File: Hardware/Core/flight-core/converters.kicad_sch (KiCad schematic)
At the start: 16 parts, among them U113 Fuse_Holder_Blade, U12 18-75V to 5V Converter, U4 TPS62086RLTR, U80 3.3V VCC Current Sensor, U81 5V VCC Current Sensor, U82 Fuse_Holder_Blade

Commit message: added common mode filter on CAN term resistor; renamed cube_ok
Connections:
- net POWER_ENABLE: now reaches U12.2 (ON/OFF)
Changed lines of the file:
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@@
+		)
+	)
+	(hierarchical_label "POWER_ENABLE"
+		(shape input)
+		(at 58.42 71.12 180)
+		(effects
+			(font
+				(size 1.27 1.27)
+			)
+			(justify right)
 		)
 	)

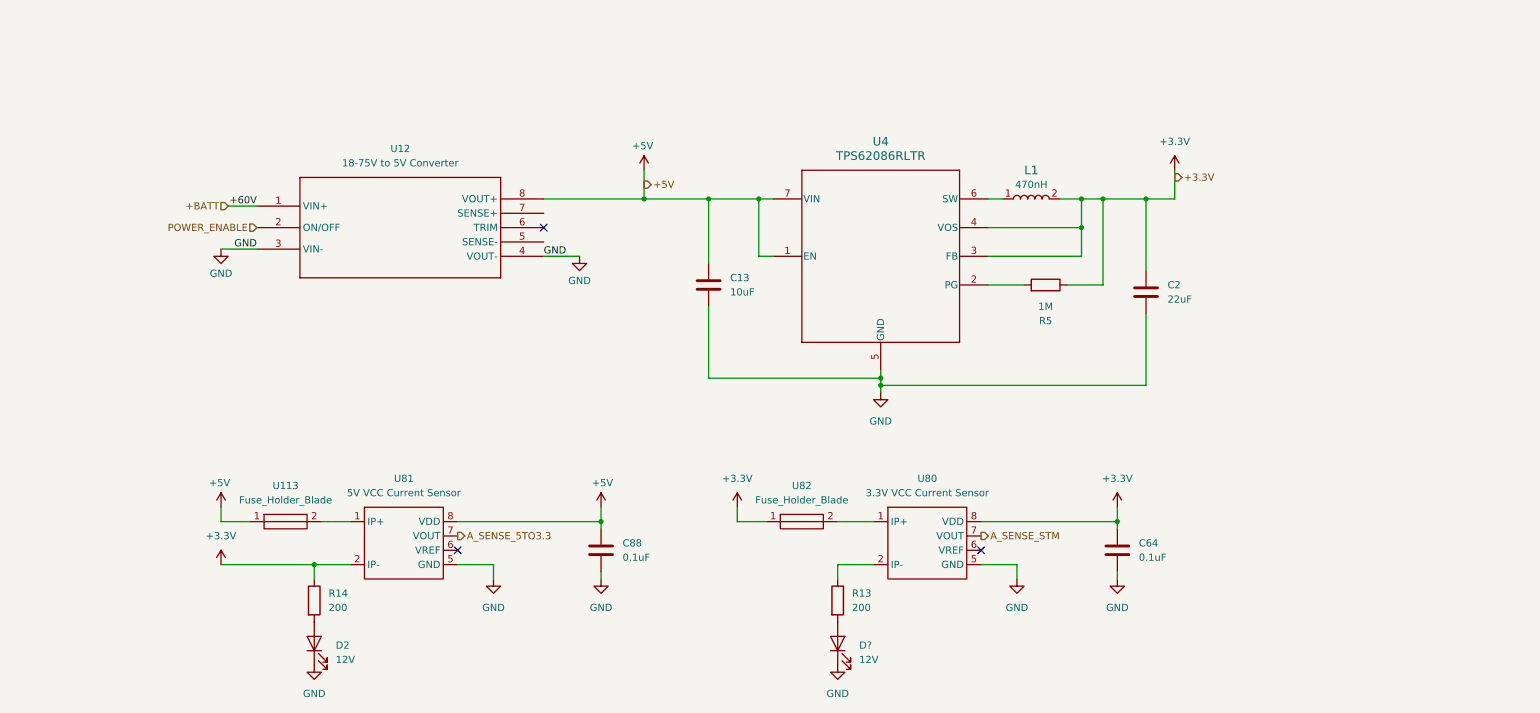
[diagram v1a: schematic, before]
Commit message: adding in-progress converter enable; in-lined shunt resistors, source 5V from USB, LEDs moved
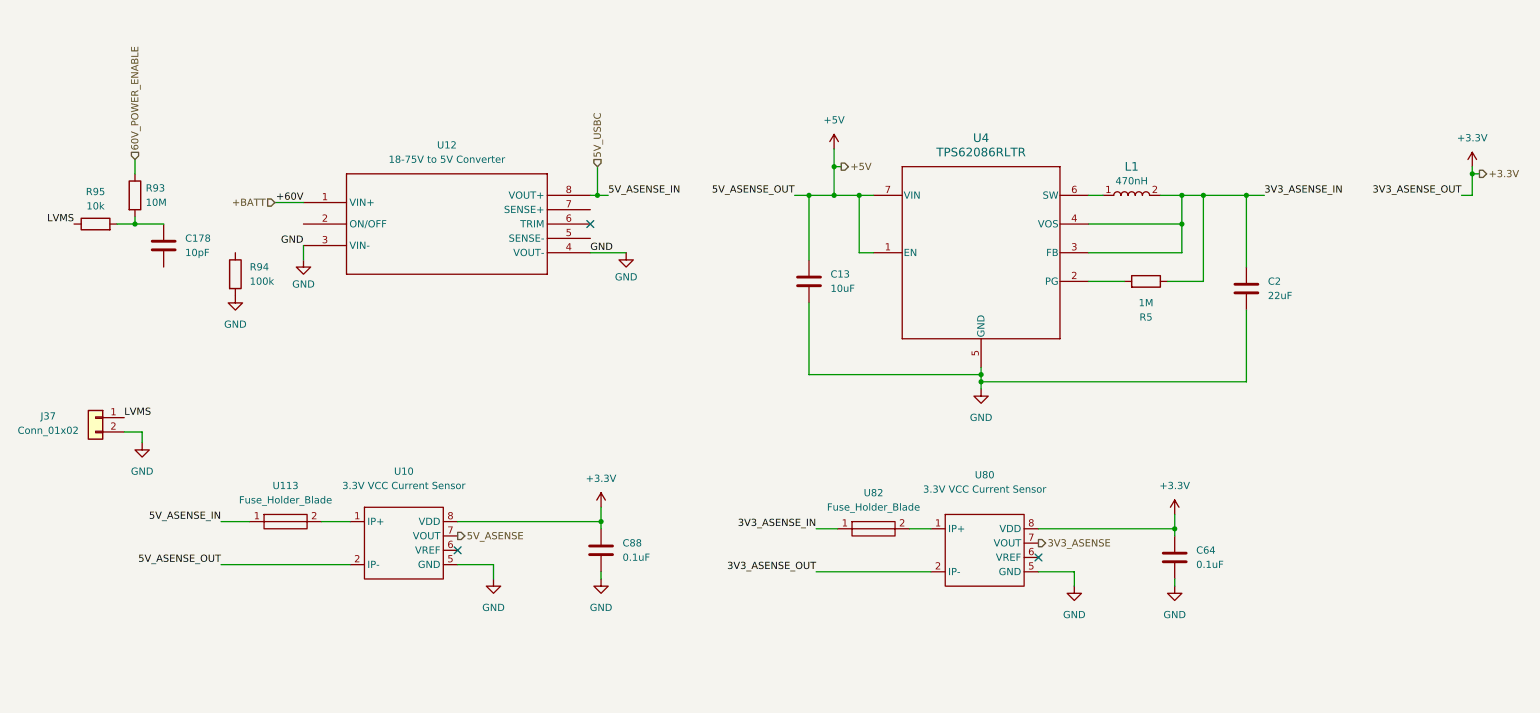
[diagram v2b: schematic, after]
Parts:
- removed D2, D?: 12V, footprints:LED_0805_OEM, symbol oem:LED_0805
- removed R13, R14: 200, OEM:R_0603, symbol OEM:R_200
- removed U81: 5V VCC Current Sensor, obad_footprints:U_Current-Sensor_ACS37010LLZATR-030B5_SOIC-6, symbol OlinBAD:ACS37010LLZATR-030B5
- added C178: 10pF, footprints:C_0603_1608Metric, symbol Device:C
- added J37: Conn_01x02, symbol Connector_Generic:Conn_01x02
- added R93: 10M, footprints:R_0603_1608Metric, symbol Device:R
- added R94: 100k, footprints:R_0603_1608Metric, symbol Device:R
- added R95: 10k, footprints:R_0603_1608Metric, symbol Device:R
- added U10: 3.3V VCC Current Sensor, obad_footprints:U_Current-Sensor_ACS37010LLZATR-030B5_SOIC-6, symbol OlinBAD:ACS37010LLZATR-030B3
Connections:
- net +3.3V: now also C88.1, U80.2 (IP-), U10.8 (VDD); no longer C2.1, L1.2, R5.1, U4.3 (FB), U4.4 (VOS), U82.1
- net +5V: now also U10.2 (IP-); no longer C88.1, U113.1, U12.8 (VOUT+)
- net GND: now also J37.2 (Pin_2), R94.2, U10.5 (GND)
- net at U113.2: now also U10.1 (IP+)
- net A_SENSE_STM renamed 3V3_ASENSE
- net POWER_ENABLE: no longer names the net of U12.2 (ON/OFF)
- new net: C178.1, R93.2, R95.2
- new net 3V3_ASENSE_IN: C2.1, L1.2, R5.1, U4.3 (FB), U4.4 (VOS), U82.1
- new net 5V_ASENSE: U10.7 (VOUT)
- new net 5V_USBC: U113.1, U12.8 (VOUT+)
- new net 60V_POWER_ENABLE: R93.1
- new net LVMS: J37.1 (Pin_1), R95.1
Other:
- moved on the sheet: C13, C2, C64, L1, R5, U12, U4, U80, U82

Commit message: top sheet reorg
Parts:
- removed J37: Conn_01x02, symbol Connector_Generic:Conn_01x02
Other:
- moved on the sheet: C13, C178, C2, C64, C88, L1, R5, R93, R94, R95, U10, U113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

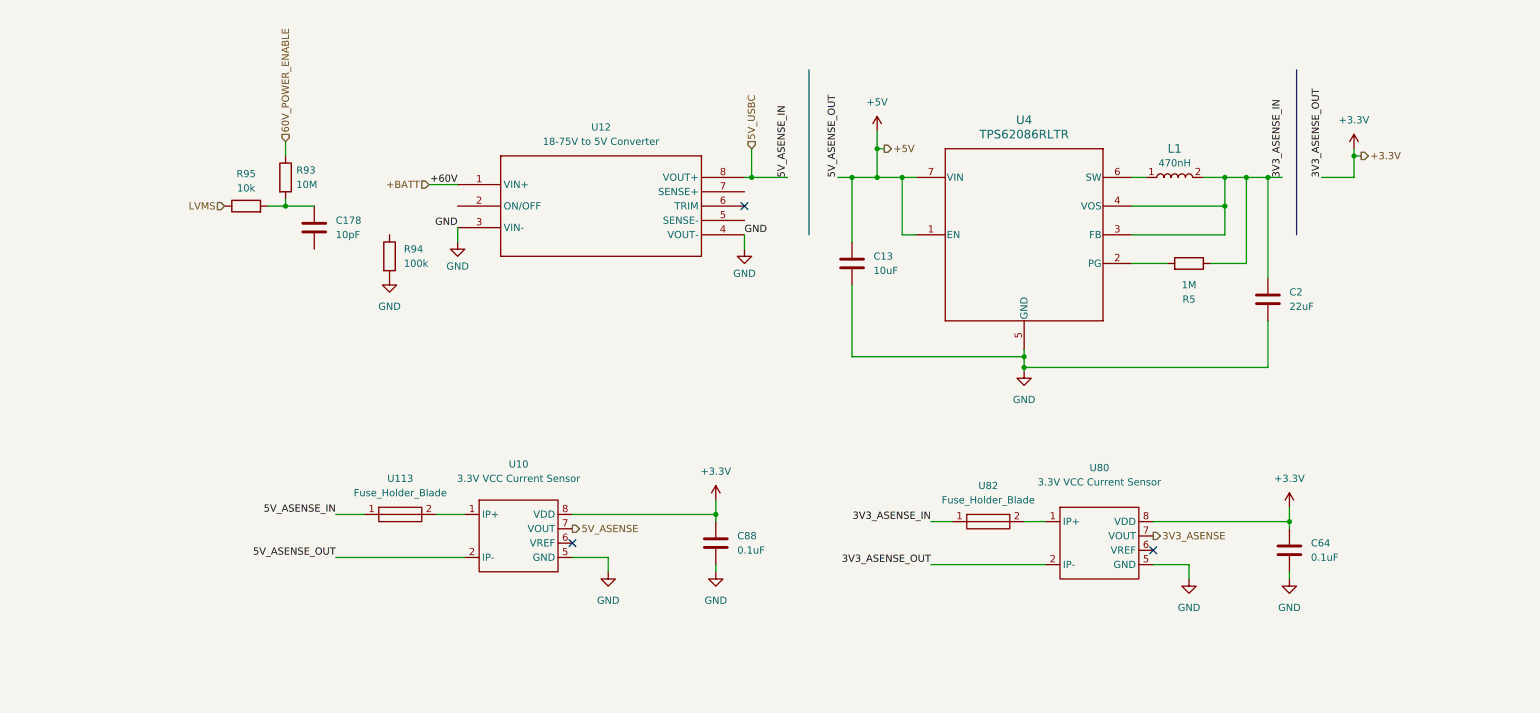
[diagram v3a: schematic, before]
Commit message: updated shutdown and some aux circuits
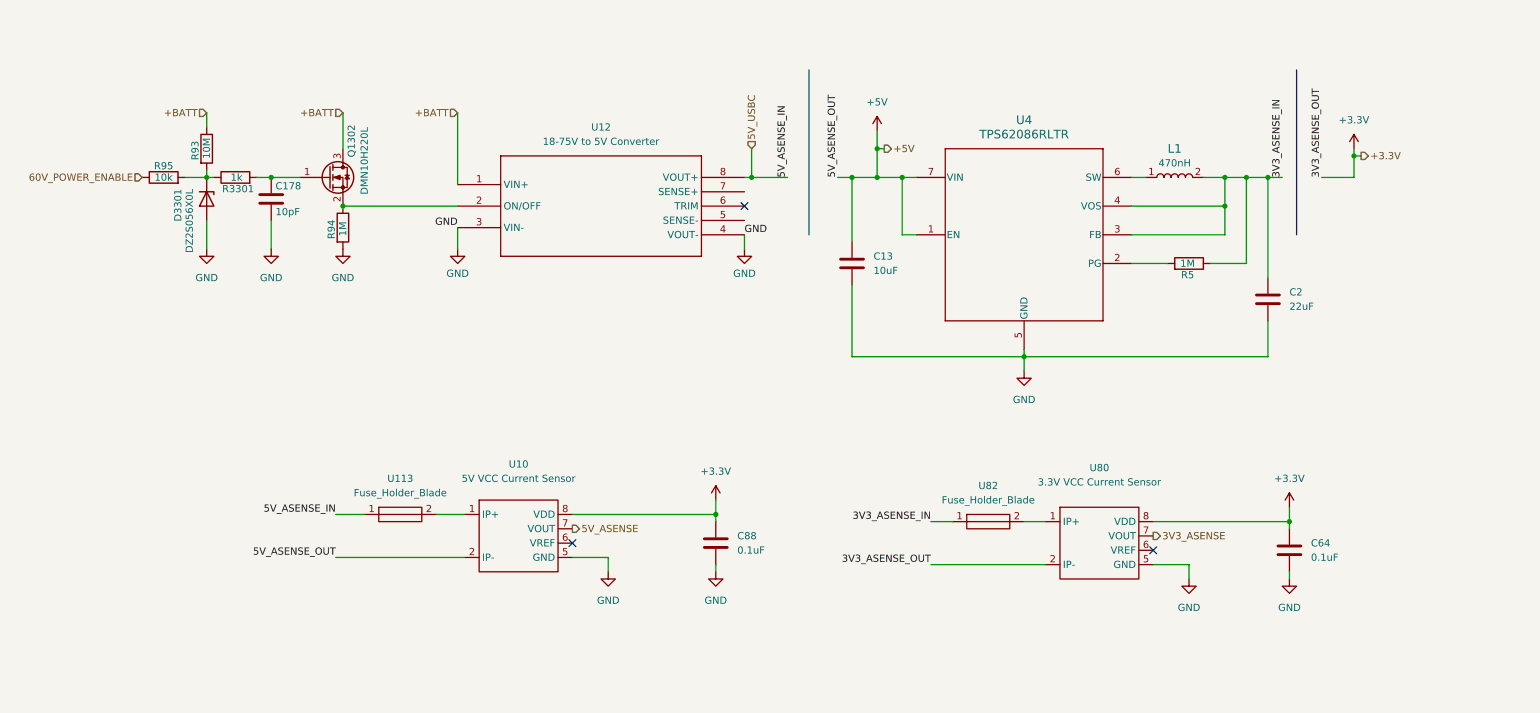
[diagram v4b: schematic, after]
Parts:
- added D3301: DZ2S056X0L, Diode_SMD:D_SOD-523, symbol Diode:DZ2S056X0L
- added Q1302: DMN10H220L, Package_TO_SOT_SMD:SOT-23, symbol Transistor_FET:DMN10H220L
- added R3301: 1k, footprints:R_0603_1608Metric, symbol Device:R
- R94: value 100k -> 1M
- U10: value 3.3V VCC Current Sensor -> 5V VCC Current Sensor
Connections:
- net LVMS is gone; now on net 60V_POWER_ENABLE: R95.1
- net +BATT: now also R93.1, Q1302.3 (D)
- net 60V_POWER_ENABLE: no longer R93.1
- net GND: now also C178.2, D3301.2 (A)
- net at R93.2, R95.2: now also D3301.1 (K), R3301.1; no longer C178.1
- net at U12.2 (ON/OFF): now also R94.1, Q1302.2 (S)
- new net: C178.1, Q1302.1 (G), R3301.2
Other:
- moved on the sheet: C178, R93, R94, R95

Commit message: updated all top sheets
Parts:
- removed R95: 10k, footprints:R_0603_1608Metric, symbol Device:R
- added R10: 1M, symbol Device:R
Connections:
- net 60V_POWER_ENABLE: now also R93.2, R10.1
- net at D3301.1 (K), R3301.1: now also R10.2; no longer R93.2
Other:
- note added: "0V"
- note added: "5.6V"
- note added: "5.6V-0.7V"
- note added: "60V"
- note added: "Grounded"
- moved on the sheet: R93
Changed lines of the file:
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@@
 	(generator_version "9.0")
 	(paper "A4")
+	(text "5.6V"
+		(exclude_from_sim no)
+		(at 64.77 59.69 0)
+		(effects
+			(font
+				(size 1.27 1.27)
+			)
+		)
+	)
+	(text "0V"
+		(exclude_from_sim no)
+		(at 83.82 69.85 0)
+		(effects
+			(font
+				(size 1.27 1.27)
+				(color 81 255 84 1)
+			)
+		)
+	)
+	(text "Grounded"
+		(exclude_from_sim no)
+		(at 22.86 52.07 0)
+		(effects
+			(font
+				(size 1.27 1.27)
+				(color 81 255 84 1)
+			)
+		)
+	)
+	(text "0V"
+		(exclude_from_sim no)
+		(at 66.04 57.15 0)
+		(effects
+			(font
+				(size 1.27 1.27)
+				(color 81 255 84 1)
+			)
+		)
+	)
+	(text "0V"
+		(exclude_from_sim no)
+		(at 52.07 52.07 0)
+		(effects
+			(font
+				(size 1.27 1.27)
+				(color 81 255 84 1)
+			)
+		)
+	)
+	(text "5.6V-0.7V"
+		(exclude_from_sim no)
+		(at 83.82 66.04 0)
+		(effects
+			(font
+				(size 1.27 1.27)
+			)
+		)
+	)
+	(text "60V"
+		(exclude_from_sim no)
+		(at 24.13 49.53 0)
+		(effects
+			(font
+				(size 1.27 1.27)
+			)
+		)
+	)
+	(text "60V"
+		(exclude_from_sim no)
+		(at 76.2 50.8 0)
+		(effects
+			(font
+				(size 1.27 1.27)
+			)
+		)
+	)
+	(text "60V"
+		(exclude_from_sim no)
+		(at 53.34 49.53 0)
+		(effects
+			(font
+				(size 1.27 1.27)
+			)
+		)
+	)
+	(text "60V"
+		(exclude_from_sim no)
+		(at 76.2 48.26 0)
+		(effects
+			(font
+				(size 1.27 1.27)
+				(color 81 255 84 1)
+			)
+		)
+	)
 	(junction
 		(at 237.49 62.23)
@@
 	(wire
 		(pts
+			(xy 49.53 39.37) (xy 49.53 40.64)
+		)
+		(stroke
+			(width 0)
+			(type default)
+		)
+	)
+	(wire
+		(pts
 			(xy 177.8 130.81) (xy 198.12 130.81)
 		)
@@
 	(wire
 		(pts
-			(xy 73.66 50.8) (xy 73.66 57.15)
+			(xy 73.66 49.53) (xy 73.66 57.15)
 		)
 		(stroke
@@
 	(wire
 		(pts
-			(xy 49.53 50.8) (xy 49.53 53.34)
-		)
-		(stroke
-			(width 0)
-			(type default)
-		)
-	)
-	(wire
-		(pts
 			(xy 168.275 57.15) (xy 168.275 62.23)
 		)
@@
 	(wire
 		(pts
+			(xy 49.53 48.26) (xy 49.53 53.34)
+		)
+		(stroke
+			(width 0)
+			(type default)
+		)
+	)
+	(wire
+		(pts
 			(xy 237.49 87.63) (xy 237.49 93.98)
 		)
@@
 		(pts
 			(xy 213.36 62.23) (xy 215.9 62.23)
-		)
-		(stroke
-			(width 0)
-			(type default)
-		)
-	)
-	(wire
-		(pts
-			(xy 45.72 62.23) (xy 49.53 62.23)
 		)
 		(stroke
@@
 		)
 	)
-	(hierarchical_label "+BATT"
-		(shape input)
-		(at 73.66 50.8 180)
-		(effects
-			(font
-				(size 1.27 1.27)
-			)
-			(justify right)
-		)
-	)
 	(hierarchical_label "3V3_ASENSE"
 		(shape output)
@@
 	(hierarchical_label "60V_POWER_ENABLE"
 		(shape input)
-		(at 38.1 62.23 180)
+		(at 49.53 50.8 180)
 		(effects
 			(font
@@
 		)
 	)
+	(hierarchical_label "+BATT"
+		(shape input)
+		(at 49.53 39.37 180)
+		(effects
+			(font
+				(size 1.27 1.27)
+			)
+			(justify right)
+		)
+	)
 	(hierarchical_label "5V_USBC"
 		(shape input)
@@
 	(hierarchical_label "+BATT"
 		(shape input)
-		(at 49.53 50.8 180)
+		(at 73.66 49.53 180)
 		(effects
 			(font
@@
 	(symbol
 		(lib_id "Device:R")
-		(at 49.53 57.15 0)
+		(at 49.53 44.45 0)
 		(unit 1)
 		(exclude_from_sim no)
@@
 		(dnp no)
 		(property "Reference" "R93"
-			(at 47.498 59.182 90)
+			(at 47.498 46.482 90)
 			(effects
 				(font
@@
 		)
 		(property "Value" "10M"
-			(at 49.53 58.928 90)
+			(at 49.53 46.228 90)
 			(effects
 				(font
@@
 		)
 		(property "Footprint" "footprints:R_0603_1608Metric"
-			(at 47.752 57.15 90)
+			(at 47.752 44.45 90)
 			(effects
 				(font
@@
 		)
 		(property "Datasheet" "~"
-			(at 49.53 57.15 0)
+			(at 49.53 44.45 0)
 			(effects
 				(font
@@
 		)
 		(property "Description" "Resistor"
-			(at 49.53 57.15 0)
+			(at 49.53 44.45 0)
 			(effects
 				(font
@@
 	(symbol
 		(lib_id "Device:R")
-		(at 41.91 62.23 90)
+		(at 49.53 57.15 0)
 		(unit 1)
 		(exclude_from_sim no)
@@
 		(on_board yes)
 		(dnp no)
-		(property "Reference" "R95"
-			(at 41.91 60.198 90)
-			(effects
-				(font
-					(size 1.27 1.27)
-				)
-			)
-		)
-		(property "Value" "10k"
-			(at 41.91 62.23 90)
-			(effects
-				(font
-					(size 1.27 1.27)
-				)
-			)
-		)
-		(property "Footprint" "footprints:R_0603_1608Metric"
-			(at 41.91 64.008 90)
+		(fields_autoplaced yes)
+		(property "Reference" "R10"
+			(at 52.07 55.8799 0)
+			(effects
+				(font
+					(size 1.27 1.27)
+				)
+				(justify left)
+			)
+		)
+		(property "Value" "1M"
+			(at 52.07 58.4199 0)
+			(effects
+				(font
+					(size 1.27 1.27)
+				)
+				(justify left)
+			)
+		)
+		(property "Footprint" ""
+			(at 47.752 57.15 90)
 			(effects
 				(font
@@
 		)
 		(property "Datasheet" "~"
-			(at 41.91 62.23 0)
+			(at 49.53 57.15 0)
 			(effects
 				(font
@@
 		)
 		(property "Description" "Resistor"
-			(at 41.91 62.23 0)
+			(at 49.53 57.15 0)
 			(effects
 				(font
@@
 			(project ""
 				(path "/93f46f4b-cdf5-47ec-af03-96378e73b2e1/f120f04e-9926-485a-8729-a726a206f3dc"
-					(reference "R95")
+					(reference "R10")
 					(unit 1)
 				)

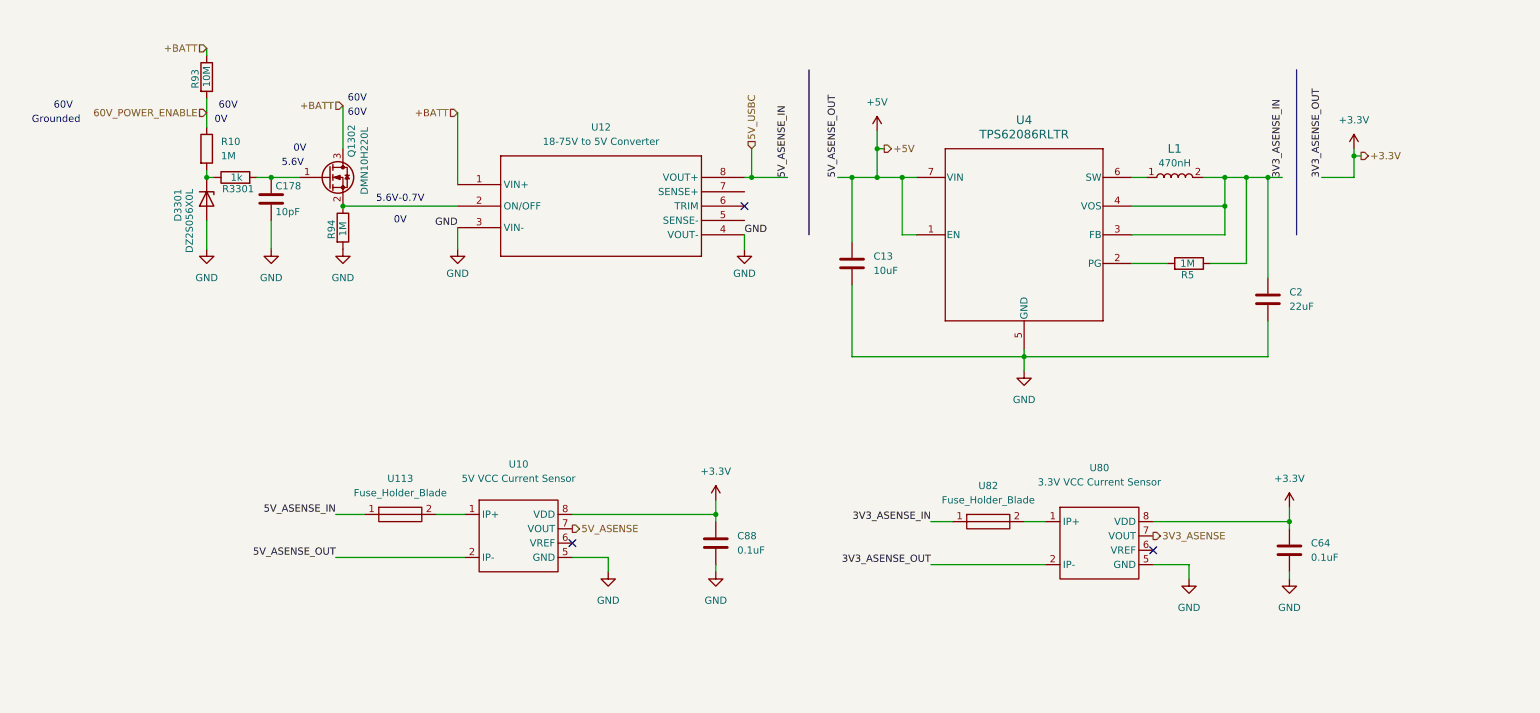
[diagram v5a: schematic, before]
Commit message: minor erc fixes (grid, reannotation, updated footprint associations)
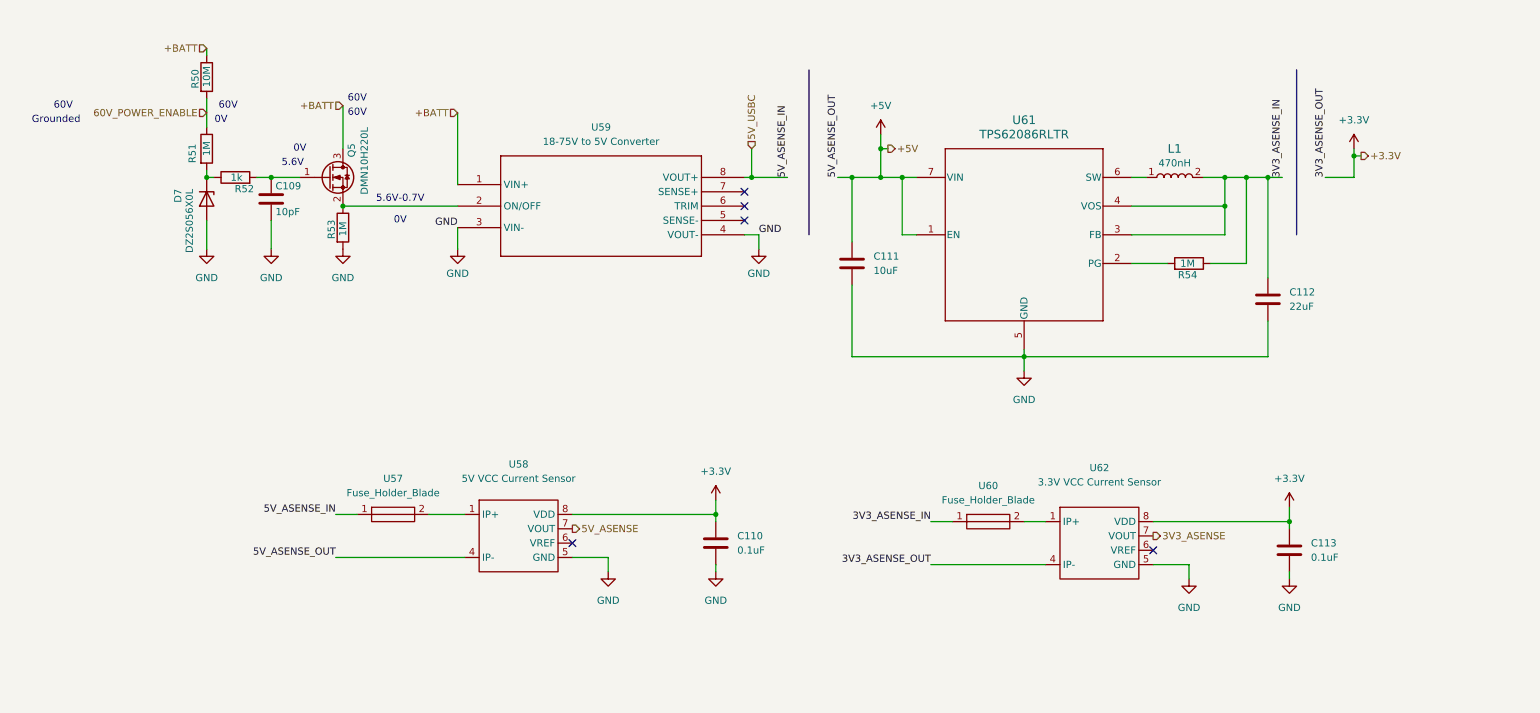
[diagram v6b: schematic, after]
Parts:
- removed U113, U82: Fuse_Holder_Blade, footprints:Fuse_Block_Holder, symbol oem:Fuse_Holder_Blade
- added U57, U60: Fuse_Holder_Blade, footprints:Fuse_Block_Holder, symbol formula:Fuse_Holder_Blade
- R51: renamed from R10; footprint (none) -> footprints:R_0603_1608Metric
- renumbered C178 to C109, C88 to C110, C13 to C111, C2 to C112, C64 to C113, D3301 to D7, Q1302 to Q5, R93 to R50, R3301 to R52, R94 to R53, R5 to R54, U10 to U58, U12 to U59, U4 to U61, U80 to U62
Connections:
- net +3.3V: now also U62.4 (IP-); no longer U62.2 (IP-)
- net +5V: now also U58.4 (IP-); no longer U58.2 (IP-)
- net 3V3_ASENSE_IN: now also U60.1
- net 5V_USBC: now also U57.1
- net at U58.1 (IP+): now also U57.2
- net at U62.1 (IP+): now also U60.2
- no-connect marks 3 -> 5
